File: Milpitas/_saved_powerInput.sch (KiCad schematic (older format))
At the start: 38 parts

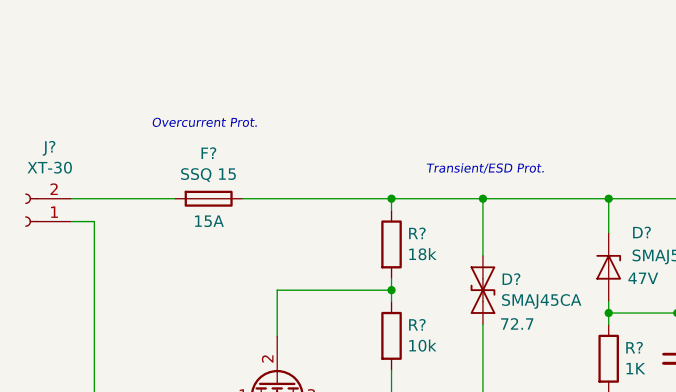
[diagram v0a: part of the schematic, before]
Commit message: Updated input control circuitry. Rationale and calcs in google drive.
Updated and added all part numbers for input protection circuitry. Not yet ready for review.
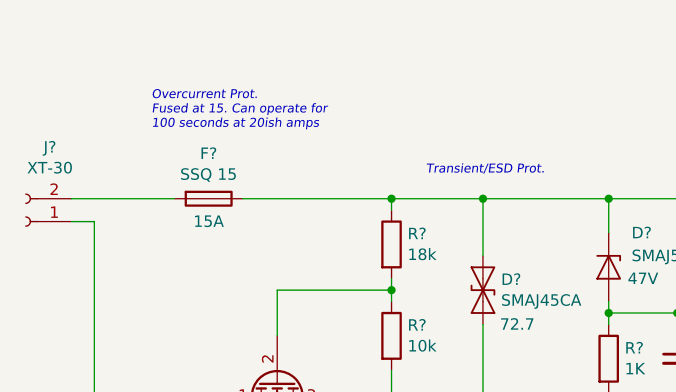
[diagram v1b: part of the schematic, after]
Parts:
- F?: I2T (none) -> 121
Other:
- note added: "Overcurrent Prot.\nFused at 15. Can operate for\n100 seconds at 20ish amps"
- note removed: "Overcurrent Prot."
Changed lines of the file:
@@
 F 4 "507-1059-1-ND" V 1350 2150 50  0001 C CNN "Digikey"
 F 5 "15A" V 1450 2150 50  0000 C CNN "Fusing Current"
+F 6 "121" V 1350 2150 50  0001 C CNN "I2T"
 	1    1350 2150
 	0    1    1    0
@@
 Transient/ESD Prot.\n
 Text Notes 1100 1850 0    39   Italic 0
-Overcurrent Prot.
+Overcurrent Prot.\nFused at 15. Can operate for\n100 seconds at 20ish amps
 Text Notes 3150 3200 0    39   Italic 0
 Overvoltage Prot
